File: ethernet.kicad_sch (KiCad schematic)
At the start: 57 parts, among them U6 KSZ9031RNXCA, Y1 ABM8G-25.000MHZ-18-D2Y-T

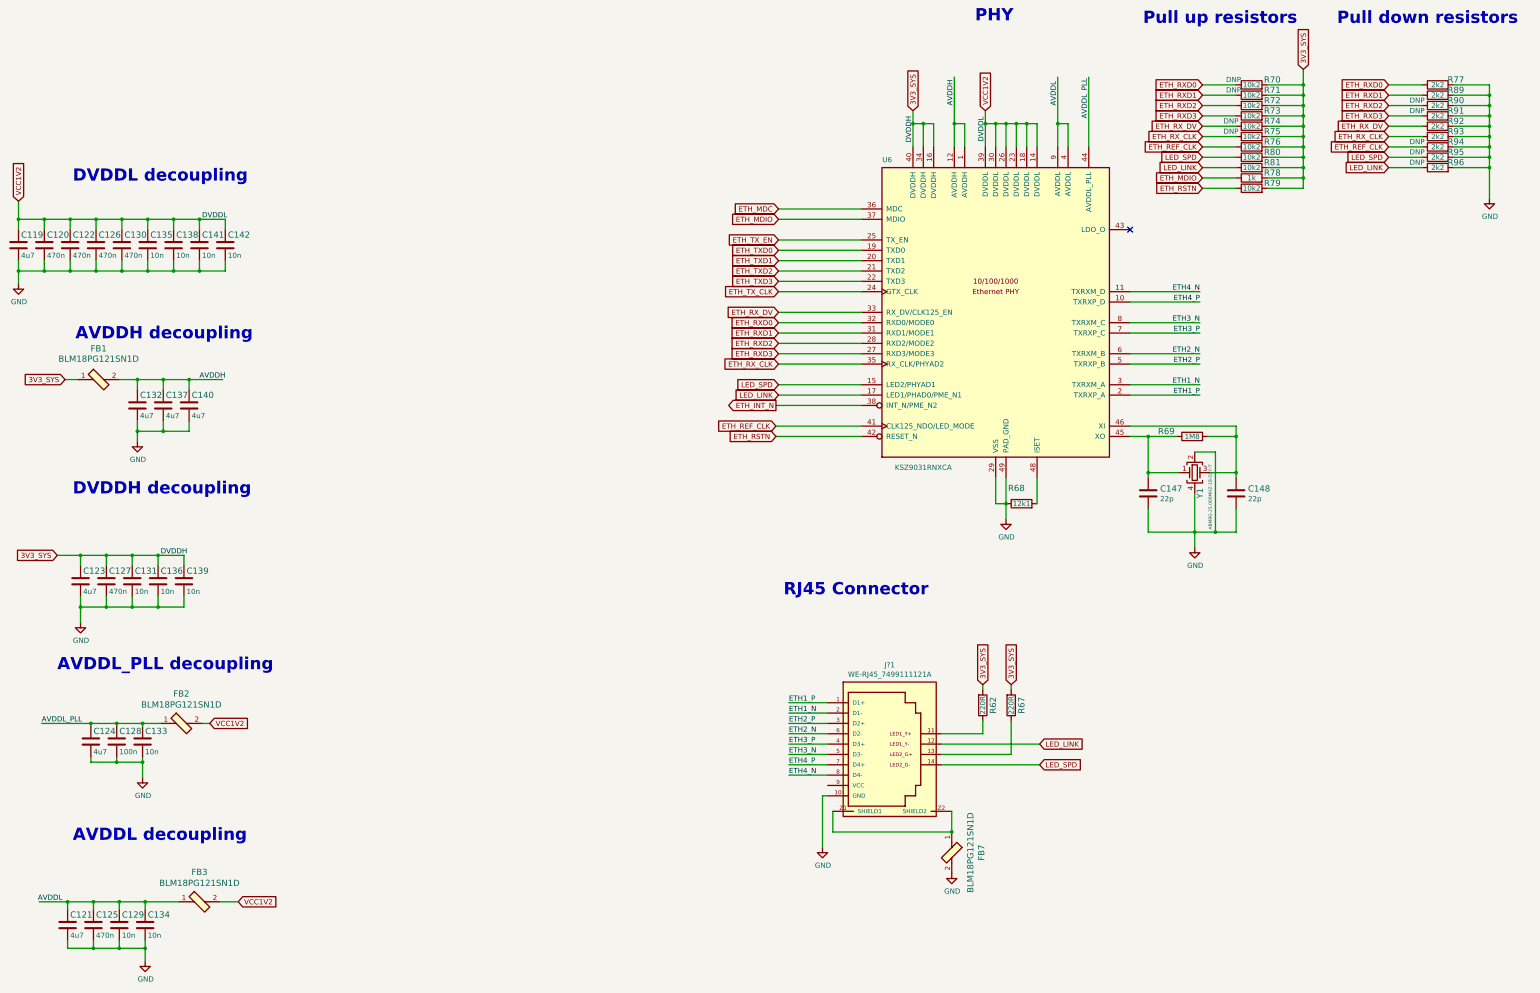
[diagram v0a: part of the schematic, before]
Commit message: Placement and routing of FT4232H. Re annotation of the schematics
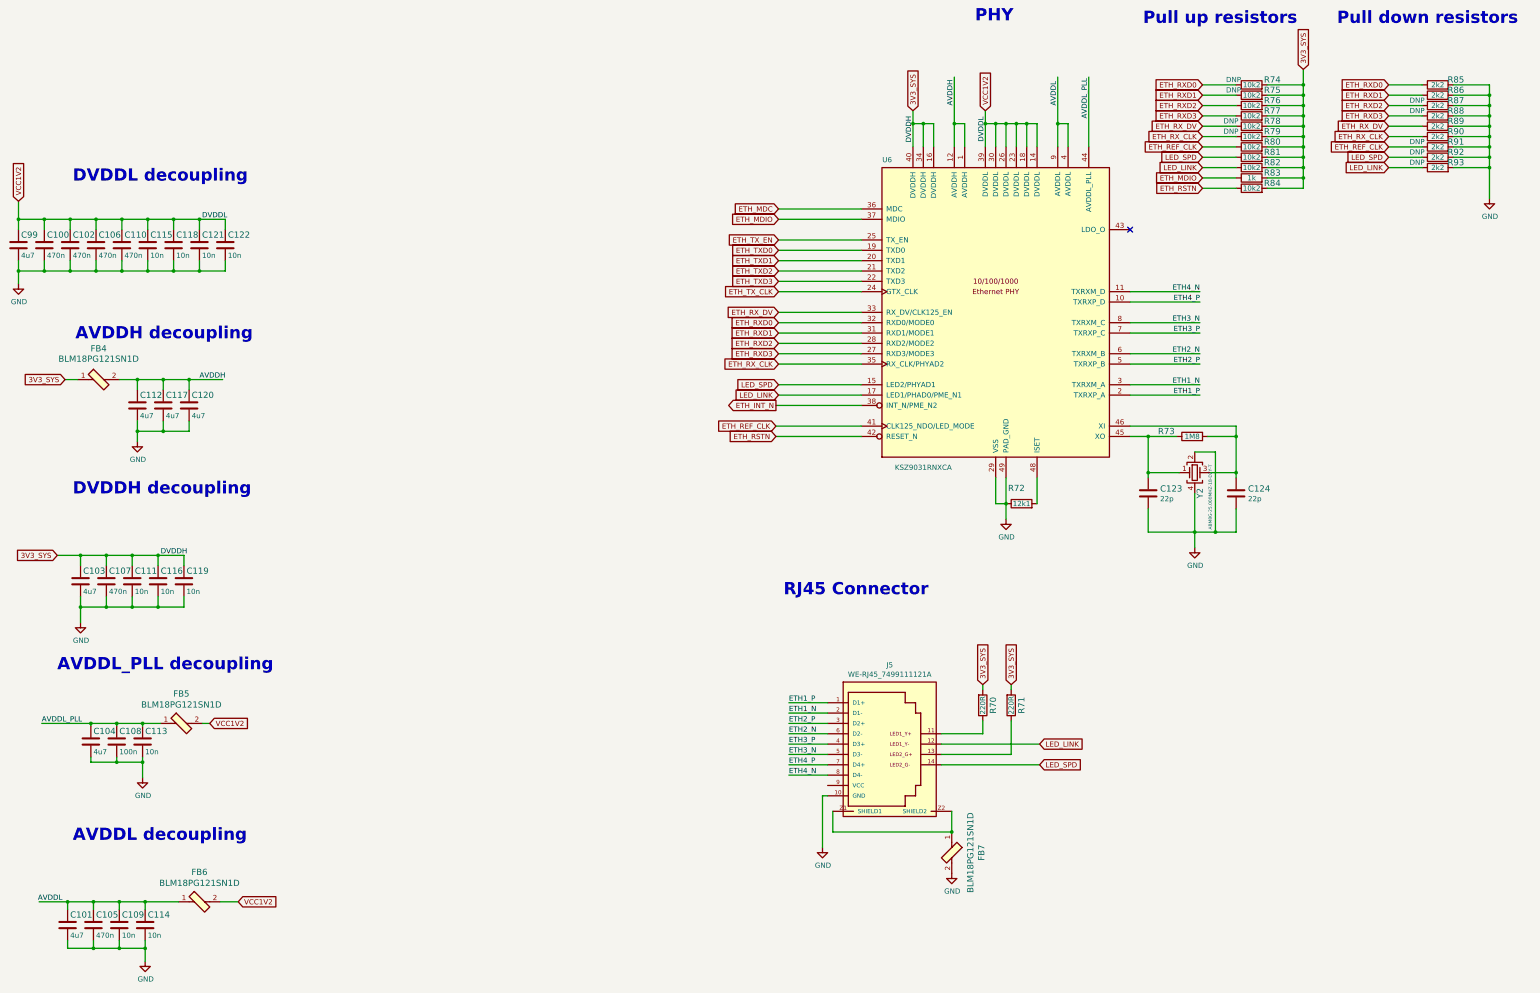
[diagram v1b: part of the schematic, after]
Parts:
- renumbered C120 to C100, C121 to C101, C122 to C102, C123 to C103, C124 to C104, C125 to C105, C126 to C106, C127 to C107, C128 to C108, C129 to C109, C130 to C110, C131 to C111, C132 to C112, C133 to C113, C134 to C114, C135 to C115, C136 to C116, C137 to C117, C138 to C118, C139 to C119, C140 to C120, C141 to C121, C142 to C122, C147 to C123, C148 to C124, C119 to C99, FB1 to FB4, FB2 to FB5, FB3 to FB6, J?1 to J5, R62 to R70, R67 to R71, R68 to R72, R69 to R73, R70 to R74, R71 to R75, R72 to R76, R73 to R77, R74 to R78, R75 to R79, R76 to R80, R80 to R81, R81 to R82, R78 to R83, R79 to R84, R77 to R85, R89 to R86, R90 to R87, R91 to R88, R92 to R89, R93 to R90, R94 to R91, R95 to R92, R96 to R93, Y1 to Y2

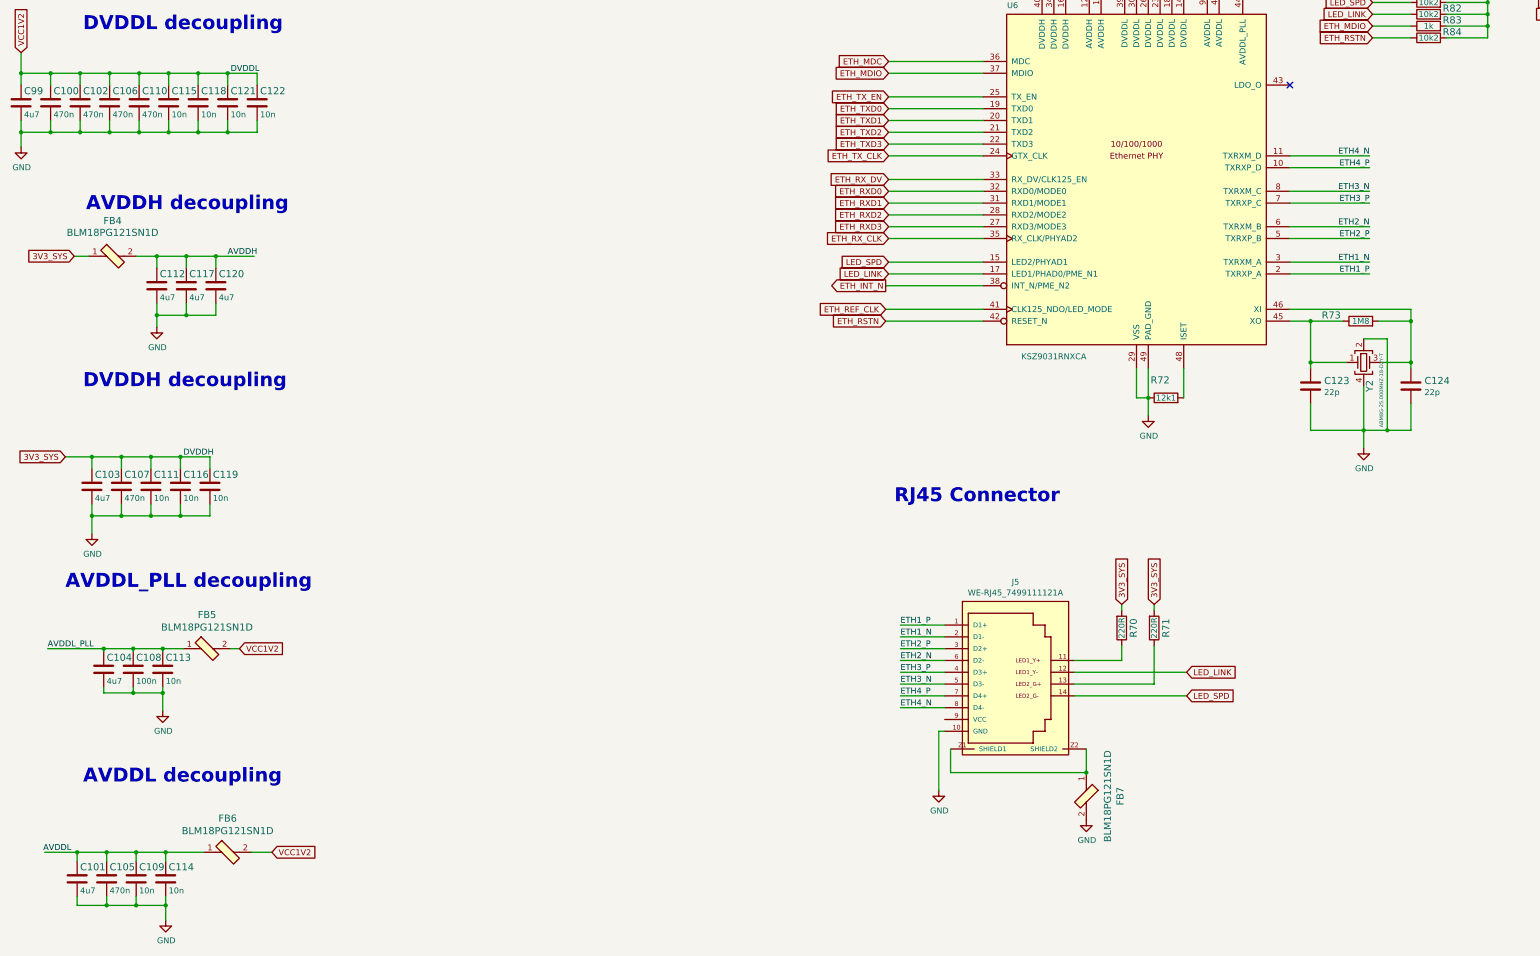
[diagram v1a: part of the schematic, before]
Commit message: Add 3d model of DDR5 testbed. Fix annotation
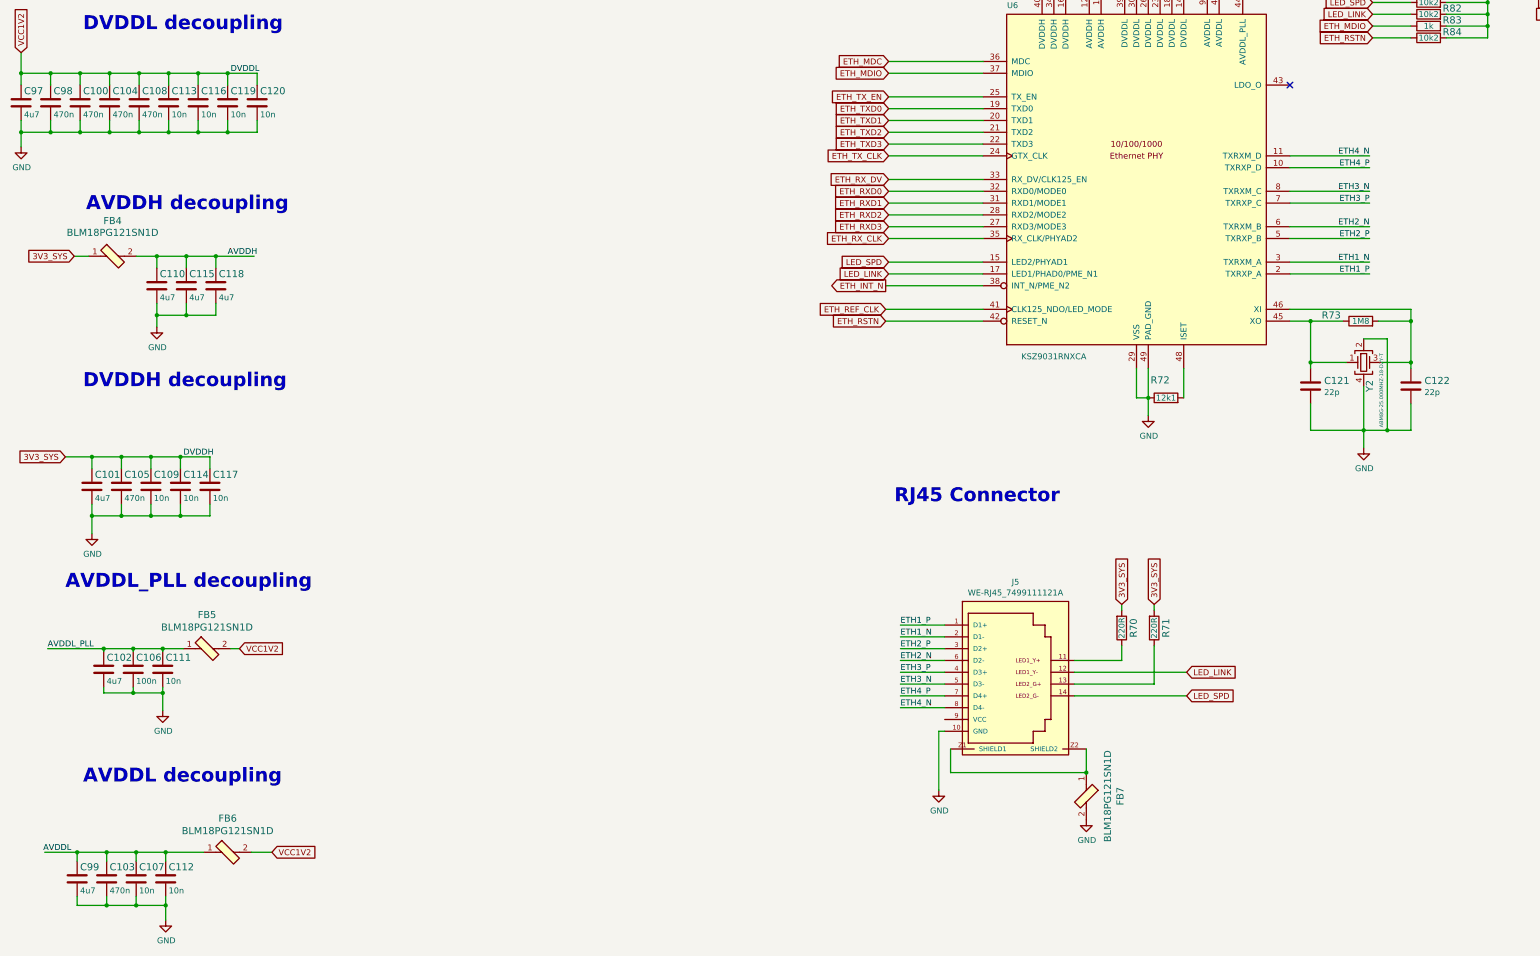
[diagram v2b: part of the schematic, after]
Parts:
- renumbered C102 to C100, C103 to C101, C104 to C102, C105 to C103, C106 to C104, C107 to C105, C108 to C106, C109 to C107, C110 to C108, C111 to C109, C112 to C110, C113 to C111, C114 to C112, C115 to C113, C116 to C114, C117 to C115, C118 to C116, C119 to C117, C120 to C118, C121 to C119, C122 to C120, C123 to C121, C124 to C122, C99 to C97, C100 to C98, C101 to C99

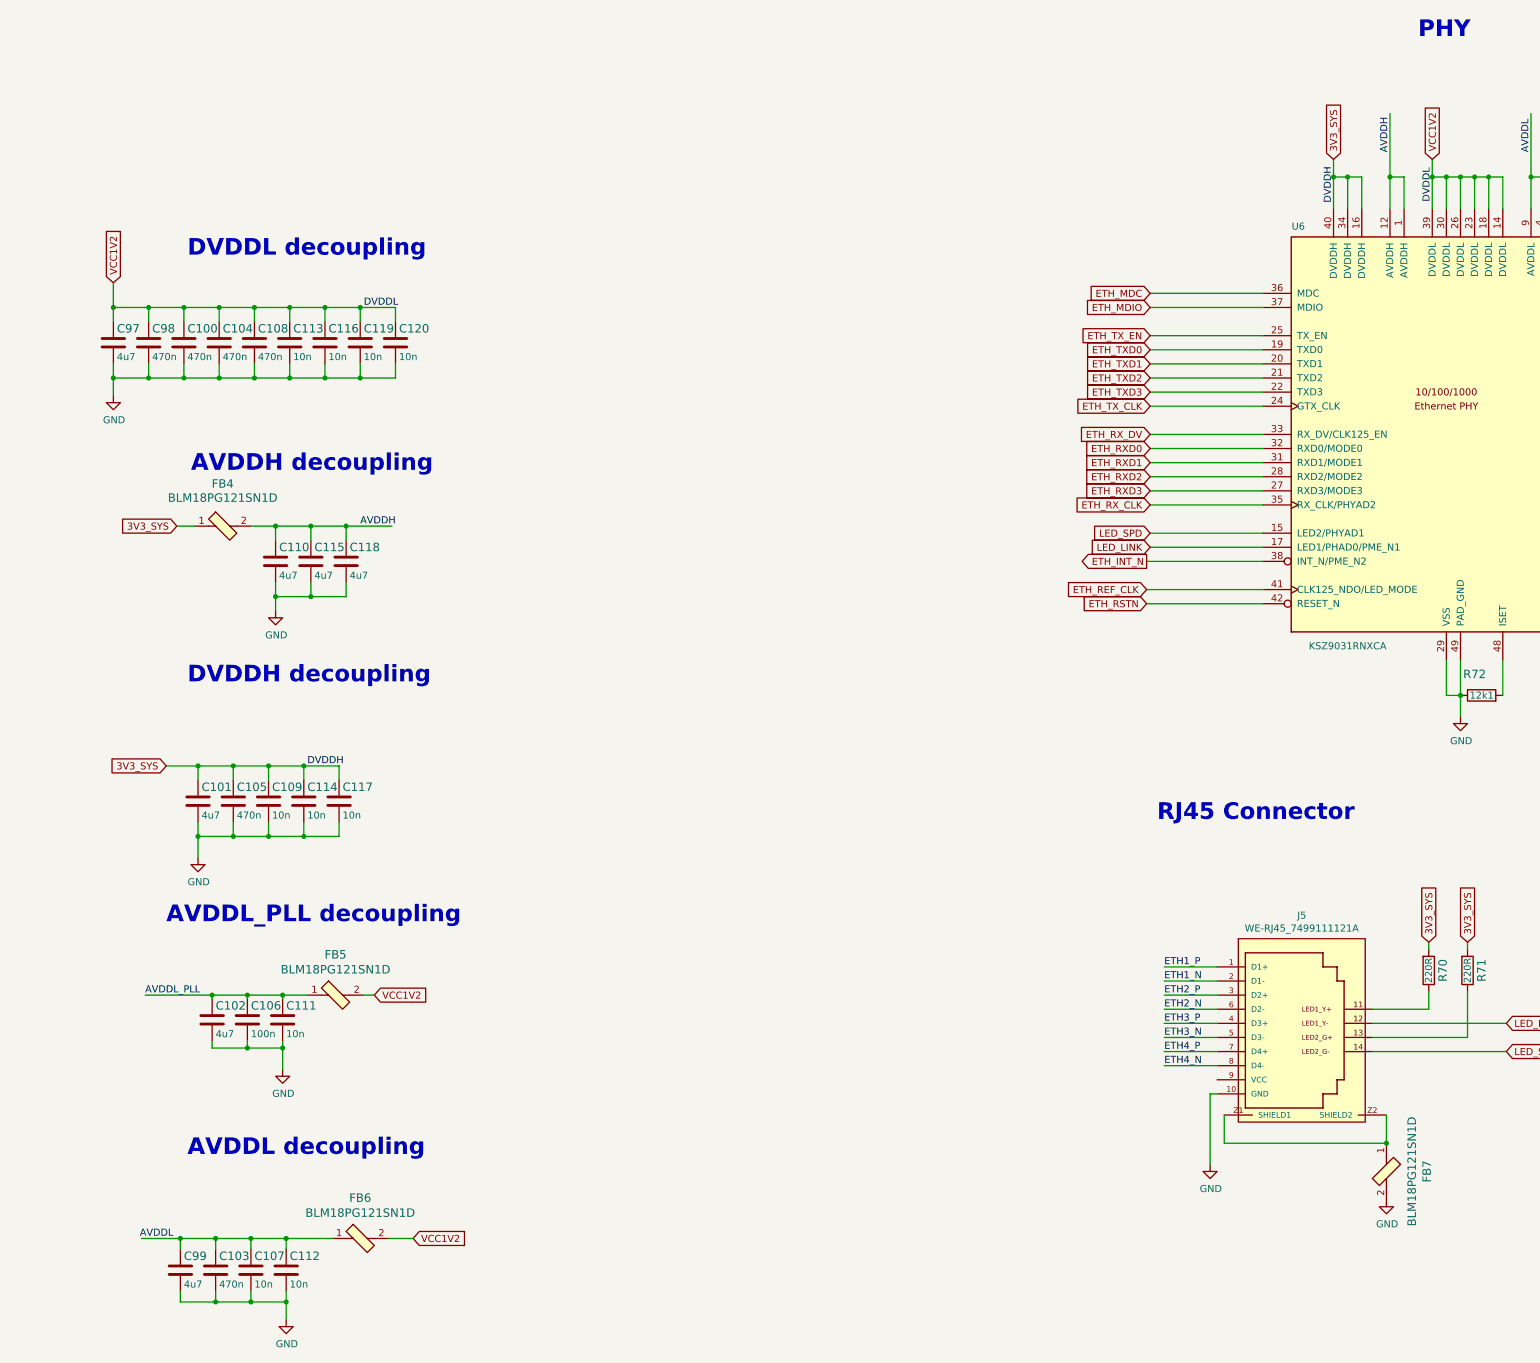
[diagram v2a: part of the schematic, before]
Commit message: Fix 1V2 power label in ethernet.sch
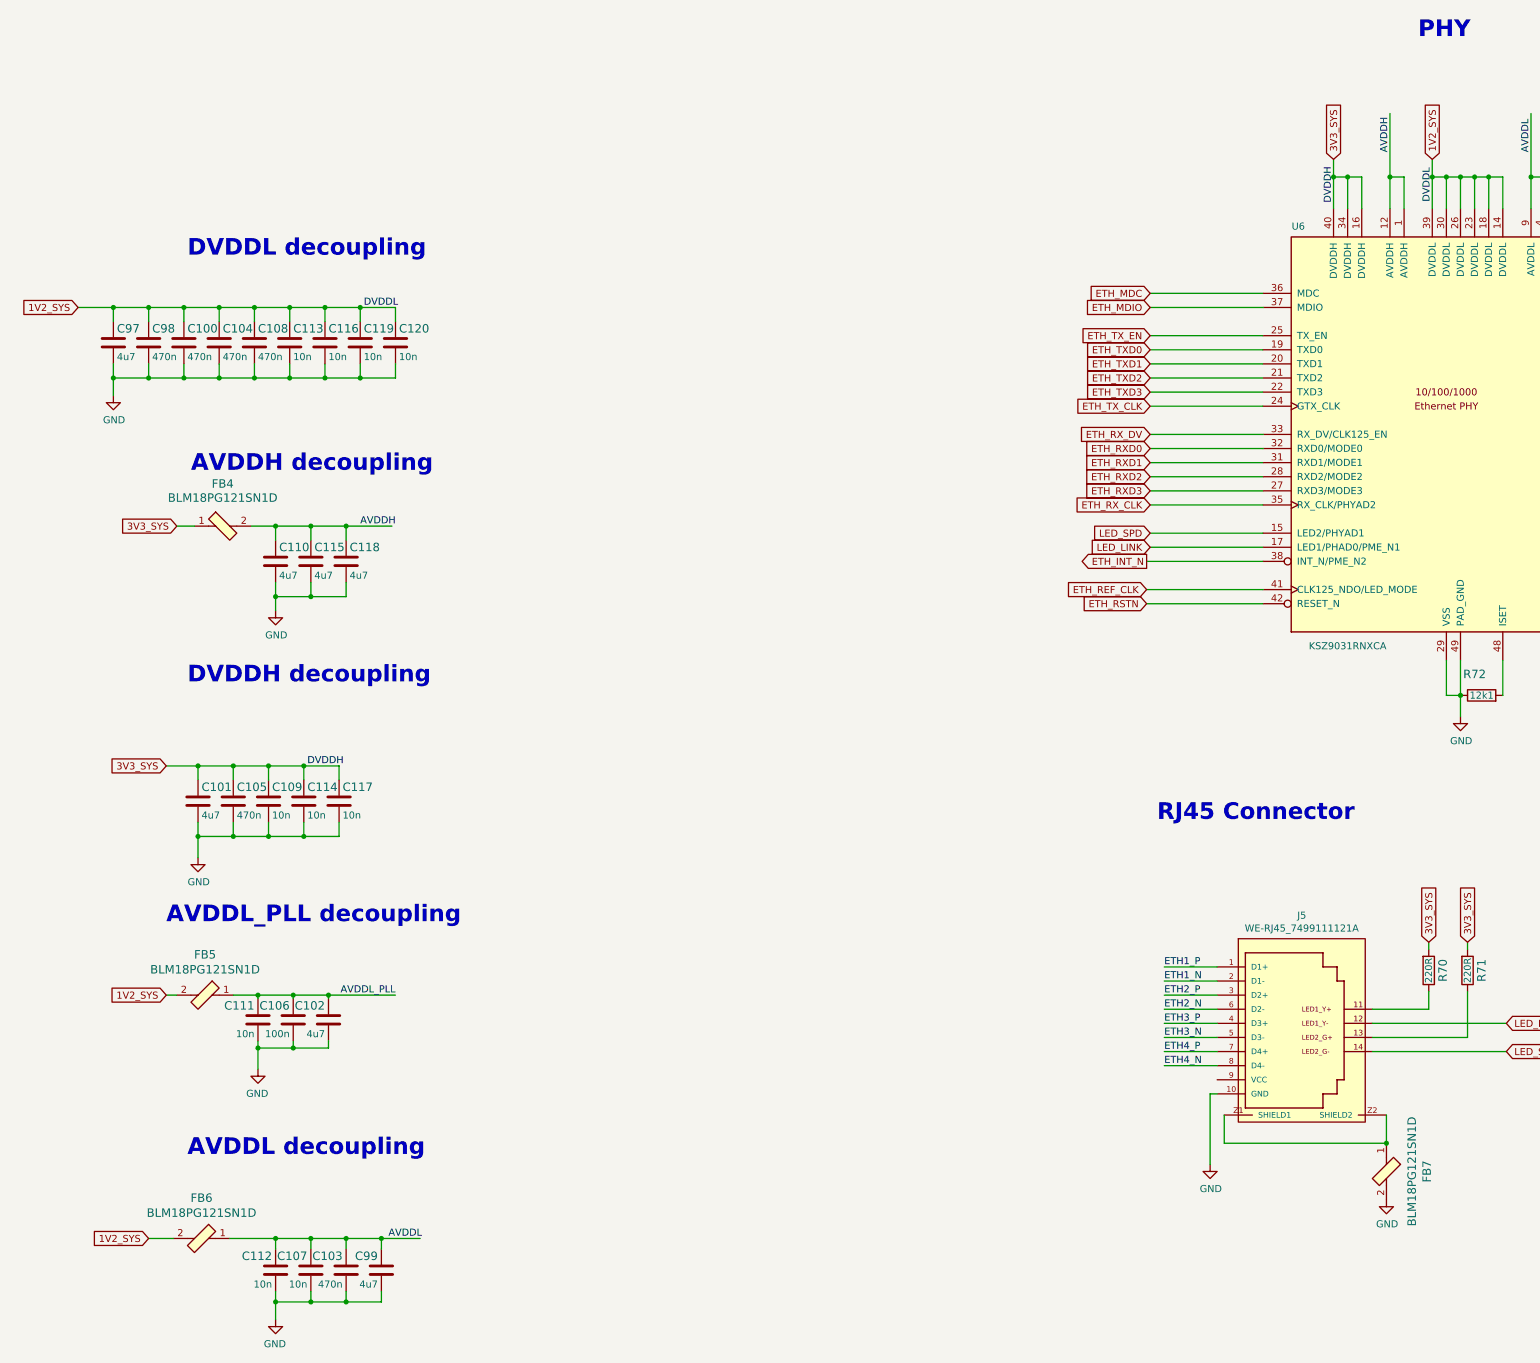
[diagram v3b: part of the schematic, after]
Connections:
- net VCC1V2 renamed 1V2_SYS
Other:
- moved on the sheet: C102, C103, C106, C107, C111, C112, C99, FB5, FB6
